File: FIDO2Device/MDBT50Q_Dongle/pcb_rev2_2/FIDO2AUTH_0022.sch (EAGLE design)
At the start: 40 parts, among them CN1 TE-1734028, CN2 IF_5PIN_H, SW1 SKRPACE010, SW2 SKTADAE010, U1 MDBT50Q-P1M, U2 XC6206P302MR-G, U4 RV-3028-C7, X1 NX3215SA-32.768K

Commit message: 回路図を修正
・LED2、LED3の配線を修正
・LED2：24（P0.08） --> 23（P0.07）
・LED3：26（P1.09） --> 16（P0.27）
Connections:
- net LED2: now also U1.P0.07; no longer U1.P0.08
- net LED3: now also U1.P0.27; no longer U1.P1.09
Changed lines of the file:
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@@
-</segment>
-</net>
-<net name="LED2" class="0">
-<segment>
-<pinref part="U1" gate="G$1" pin="P0.08"/>
-<wire x1="73.66" y1="45.72" x2="73.66" y2="12.7" width="0.1524" layer="91"/>
-<wire x1="73.66" y1="12.7" x2="104.14" y2="12.7" width="0.1524" layer="91"/>
-<label x="104.14" y="12.7" size="1.778" layer="95" xref="yes"/>
-</segment>
-</net>
-<net name="LED3" class="0">
-<segment>
-<pinref part="U1" gate="G$1" pin="P1.09"/>
-<wire x1="78.74" y1="45.72" x2="78.74" y2="17.78" width="0.1524" layer="91"/>
-<wire x1="78.74" y1="17.78" x2="104.14" y2="17.78" width="0.1524" layer="91"/>
-<label x="104.14" y="17.78" size="1.778" layer="95" xref="yes"/>
 </segment>
 </net>
@@
 </segment>
 </net>
+<net name="LED3" class="0">
+<segment>
+<pinref part="U1" gate="G$1" pin="P0.27"/>
+<wire x1="53.34" y1="45.72" x2="53.34" y2="38.1" width="0.1524" layer="91"/>
+<wire x1="53.34" y1="38.1" x2="40.64" y2="38.1" width="0.1524" layer="91"/>
+<label x="40.64" y="38.1" size="1.778" layer="95" rot="R180" xref="yes"/>
+</segment>
+</net>
+<net name="LED2" class="0">
+<segment>
+<pinref part="U1" gate="G$1" pin="P0.07"/>
+<wire x1="71.12" y1="45.72" x2="71.12" y2="17.78" width="0.1524" layer="91"/>
+<wire x1="71.12" y1="17.78" x2="104.14" y2="17.78" width="0.1524" layer="91"/>
+<label x="104.14" y="17.78" size="1.778" layer="95" xref="yes"/>
+</segment>
+</net>

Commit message: 回路図を修正
・部品番号を振り直し
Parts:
- removed LD1: APTD1608LSECK/J4-PF, Parts:APTD1608LSECK/J4-PF
- removed LD2: APHD1608LSURCK, Parts:APHD1608LSURCK
- removed LD3: APTD1608LZGCK, Parts:APTD1608LZGCK
- removed R11: 10k, Parts:RESISTOR_0402N
- added D5: PRTR5V0U2X, Parts:PRTR5V0U2X
- added D6, D7: PMEG2005AEA,115, Parts:PMEG2005AEA,115
- added R7: 10k, Parts:RESISTOR_0402N
- C5: value 0.01uF -> 0.1uF
- C6: value 10uF -> 0.01uF; device Parts:CAP_0603N -> Parts:CAP_0402N
- C9: value 0.1uF -> 10uF; device Parts:CAP_0402N -> Parts:CAP_0603N
- D1: value PRTR5V0U2X -> APTD1608LSECK/J4-PF; device Parts:PRTR5V0U2X -> Parts:APTD1608LSECK/J4-PF
- D2: value PMEG2005AEA,115 -> APHD1608LSURCK; device Parts:PMEG2005AEA,115 -> Parts:APHD1608LSURCK
- D3: value PMEG2005AEA,115 -> APTD1608LZGCK; device Parts:PMEG2005AEA,115 -> Parts:APTD1608LZGCK
- R2: value 10k -> 1.2k
- R6: value 1.2k -> 10k
- renumbered C13 to C12, FB1 to L1, FB2 to L2, FB3 to L3, LD4 to D4, R10 to R8, U4 to U3
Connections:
- net 0V: now also D5.GND, R9.1; no longer D1.GND, R11.1
- net D_N: now also D5.I/O_1; no longer D1.I/O_1
- net D_P: now also D5.I/O_2; no longer D1.I/O_2
- net LED1: now also R2.1; no longer R6.1
- net N$4: now also D6.A; no longer D2.A
- net N$5: now also D7.A; no longer D3.A
- net N$6: now also D3.C; no longer LD3.C
- net N$7: now also D2.C; no longer LD2.C
- net N$8: now also D1.C, R2.2; no longer LD1.C, R6.2
- net N$9: now also R9.2; no longer R11.2
- net RESET: now also C5.1; no longer C9.1
- net TWI_SCL: now also R7.1; no longer R9.1
- net TWI_SDA: now also R6.1; no longer R2.1
- net VBUS: now also C9.1, D5.VCC; no longer C5.1, D1.VCC
- net VDD_NRF: now also D1.A, D2.A, D3.A, D6.C, D7.C, R6.2, R7.2; no longer D2.C, D3.C, LD1.A, LD2.A, LD3.A, R2.2, R9.2
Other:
- note added: "USBポートに装着時は、VBUSの5.0V-->3.0Vに降圧して供給します。 乾電池ホルダーにボタン乾電池を装着した場合は、3.0Vを供給します。"
- note removed: "USBポートに装着時は、VBUSの5.0V-->3.3Vに降圧して供給します。 乾電池ホルダーにボタン乾電池を装着した場合は、3.0Vを供給します。"

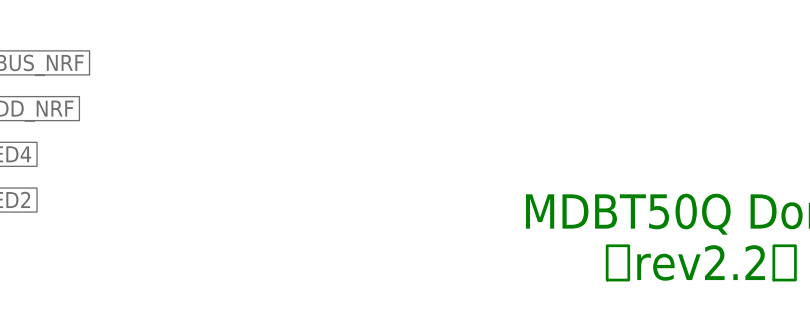
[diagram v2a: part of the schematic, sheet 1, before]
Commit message: 捨て板設定を追加
・認識マークを捨て板上に４点追加
・回路図を修正
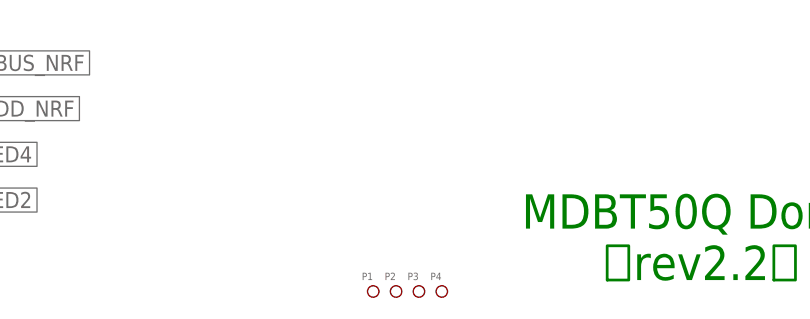
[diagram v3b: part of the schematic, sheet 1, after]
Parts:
- added P1, P2, P3, P4: 0, Generic:PAD-MARK
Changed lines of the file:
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@@
 <part name="R9" library="Parts" deviceset="RESISTOR" device="_0402N" value="10k"/>
 <part name="CN2" library="Connectors" deviceset="IF_5PIN" device="_H"/>
+<part name="P1" library="Generic" deviceset="PAD-MARK" device="" value="0"/>
+<part name="P2" library="Generic" deviceset="PAD-MARK" device="" value="0"/>
+<part name="P3" library="Generic" deviceset="PAD-MARK" device="" value="0"/>
+<part name="P4" library="Generic" deviceset="PAD-MARK" device="" value="0"/>
 </parts>
 <sheets>
@@
 </instance>
 <instance part="GND12" gate="1" x="210.82" y="63.5"/>
+<instance part="P1" gate="G$1" x="149.86" y="7.62"/>
+<instance part="P2" gate="G$1" x="152.4" y="7.62"/>
+<instance part="P3" gate="G$1" x="154.94" y="7.62"/>
+<instance part="P4" gate="G$1" x="157.48" y="7.62"/>
 </instances>
 <busses>
